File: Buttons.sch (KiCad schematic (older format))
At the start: 24 parts, among them SW1 SW_PUSHBUTTON, SW2 SW_PUSHBUTTON, SW3 SW_PUSHBUTTON, SW4 SW_PUSHBUTTON, SW5 SW_PUSHBUTTON, SW6 SW_PUSHBUTTON

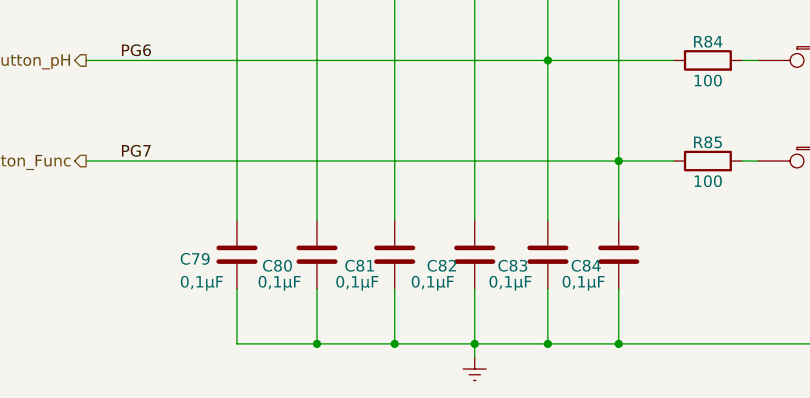
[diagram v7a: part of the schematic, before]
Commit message: corrected few footprints, correct all resistors and capacitors type for ordering
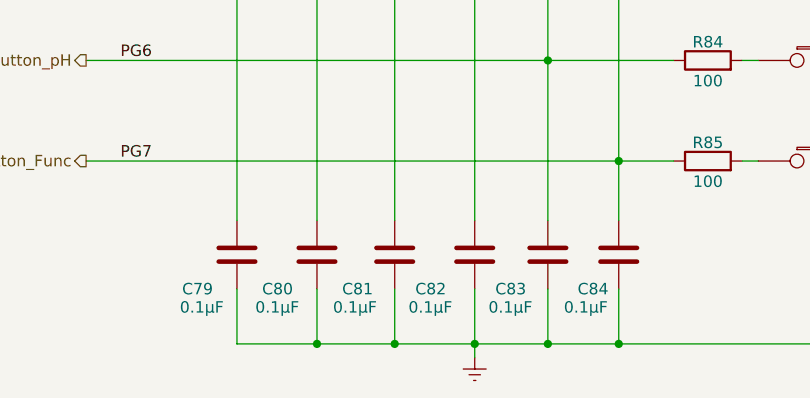
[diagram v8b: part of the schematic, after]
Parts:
- C79, C81, C82, C83, C84: value 0,1µF -> 0.1µF; Type C0603C104K5RACTU -> CL10B104KC8NNNC
- C80: value 0,1µF -> 0.1µF; Type CL10B105KA8NNNC -> CL10B104KC8NNNC
- R74, R75, R76, R77, R78, R79: Type (none) -> RC0805FR-0715KL
- R80, R81, R82, R83, R84, R85: Type (none) -> RC0805FR-07100RL
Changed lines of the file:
@@
 F 2 "Resistor_SMD:R_0805_2012Metric_Pad1.20x1.40mm_HandSolder" V 5930 1480 50  0001 C CNN
 F 3 "~" H 6000 1480 50  0001 C CNN
+F 4 "RC0805FR-0715KL" H 6000 1480 50  0001 C CNN "Type"
 	1    6000 1480
 	1    0    0    -1
@@
 F 2 "Resistor_SMD:R_0805_2012Metric_Pad1.20x1.40mm_HandSolder" V 5620 1480 50  0001 C CNN
 F 3 "~" H 5690 1480 50  0001 C CNN
+F 4 "RC0805FR-0715KL" H 5690 1480 50  0001 C CNN "Type"
 	1    5690 1480
 	1    0    0    -1
@@
 F 2 "Resistor_SMD:R_0805_2012Metric_Pad1.20x1.40mm_HandSolder" V 5300 1480 50  0001 C CNN
 F 3 "~" H 5370 1480 50  0001 C CNN
+F 4 "RC0805FR-0715KL" H 5370 1480 50  0001 C CNN "Type"
 	1    5370 1480
 	1    0    0    -1
@@
 F 2 "Resistor_SMD:R_0805_2012Metric_Pad1.20x1.40mm_HandSolder" V 4950 1480 50  0001 C CNN
 F 3 "~" H 5020 1480 50  0001 C CNN
+F 4 "RC0805FR-0715KL" H 5020 1480 50  0001 C CNN "Type"
 	1    5020 1480
 	1    0    0    -1
@@
 F 2 "Resistor_SMD:R_0805_2012Metric_Pad1.20x1.40mm_HandSolder" V 4610 1480 50  0001 C CNN
 F 3 "~" H 4680 1480 50  0001 C CNN
+F 4 "RC0805FR-0715KL" H 4680 1480 50  0001 C CNN "Type"
 	1    4680 1480
 	1    0    0    -1
@@
 F 2 "Resistor_SMD:R_0805_2012Metric_Pad1.20x1.40mm_HandSolder" V 4260 1480 50  0001 C CNN
 F 3 "~" H 4330 1480 50  0001 C CNN
+F 4 "RC0805FR-0715KL" H 4330 1480 50  0001 C CNN "Type"
 	1    4330 1480
 	1    0    0    -1
@@
 F 2 "Resistor_SMD:R_0805_2012Metric_Pad1.20x1.40mm_HandSolder" V 6310 2030 50  0001 C CNN
 F 3 "~" H 6380 2030 50  0001 C CNN
+F 4 "RC0805FR-07100RL" V 6380 2030 50  0001 C CNN "Type"
 	1    6380 2030
 	0    -1   -1   0
@@
 AR Path="/60D8C564/60D436EA" Ref="C?"  Part="1"
 AR Path="/60CDBD15/60D436EA" Ref="C79"  Part="1"
-F 0 "C79" H 4080 4620 50  0000 L CNN
-F 1 "0,1µF" H 4080 4520 50  0000 L CNN
+F 0 "C79" H 4090 4490 50  0000 L CNN
+F 1 "0.1µF" H 4080 4410 50  0000 L CNN
 F 2 "Capacitor_SMD:C_0603_1608Metric_Pad1.08x0.95mm_HandSolder" H 4368 4490 50  0001 C CNN
 F 3 "http://www.farnell.com/datasheets/2710676.pdf" H 4330 4640 50  0001 C CNN
-F 4 "C0603C104K5RACTU" H 4330 4640 50  0001 C CNN "Type"
+F 4 "CL10B104KC8NNNC" H 4330 4640 50  0001 C CNN "Type"
 	1    4330 4640
 	1    0    0    -1
@@
 AR Path="/60D8C564/60D44563" Ref="C?"  Part="1"
 AR Path="/60CDBD15/60D44563" Ref="C80"  Part="1"
-F 0 "C80" H 4440 4590 50  0000 L CNN
-F 1 "0,1µF" H 4420 4520 50  0000 L CNN
+F 0 "C80" H 4440 4490 50  0000 L CNN
+F 1 "0.1µF" H 4410 4410 50  0000 L CNN
 F 2 "Capacitor_SMD:C_0603_1608Metric_Pad1.08x0.95mm_HandSolder" H 4718 4490 50  0001 C CNN
 F 3 "http://www.farnell.com/datasheets/2710676.pdf" H 4680 4640 50  0001 C CNN
-F 4 "CL10B105KA8NNNC" H 4680 4640 50  0001 C CNN "Type"
+F 4 "CL10B104KC8NNNC" H 4680 4640 50  0001 C CNN "Type"
 	1    4680 4640
 	1    0    0    -1
@@
 AR Path="/60D8C564/60D44905" Ref="C?"  Part="1"
 AR Path="/60CDBD15/60D44905" Ref="C81"  Part="1"
-F 0 "C81" H 4800 4590 50  0000 L CNN
-F 1 "0,1µF" H 4760 4520 50  0000 L CNN
+F 0 "C81" H 4790 4490 50  0000 L CNN
+F 1 "0.1µF" H 4750 4410 50  0000 L CNN
 F 2 "Capacitor_SMD:C_0603_1608Metric_Pad1.08x0.95mm_HandSolder" H 5058 4490 50  0001 C CNN
 F 3 "http://www.farnell.com/datasheets/2710676.pdf" H 5020 4640 50  0001 C CNN
-F 4 "C0603C104K5RACTU" H 5020 4640 50  0001 C CNN "Type"
+F 4 "CL10B104KC8NNNC" H 5020 4640 50  0001 C CNN "Type"
 	1    5020 4640
 	1    0    0    -1
@@
 AR Path="/60D8C564/60D44D94" Ref="C?"  Part="1"
 AR Path="/60CDBD15/60D44D94" Ref="C82"  Part="1"
-F 0 "C82" H 5160 4590 50  0000 L CNN
-F 1 "0,1µF" H 5090 4520 50  0000 L CNN
+F 0 "C82" H 5110 4490 50  0000 L CNN
+F 1 "0.1µF" H 5080 4410 50  0000 L CNN
 F 2 "Capacitor_SMD:C_0603_1608Metric_Pad1.08x0.95mm_HandSolder" H 5408 4490 50  0001 C CNN
 F 3 "http://www.farnell.com/datasheets/2710676.pdf" H 5370 4640 50  0001 C CNN
-F 4 "C0603C104K5RACTU" H 5370 4640 50  0001 C CNN "Type"
+F 4 "CL10B104KC8NNNC" H 5370 4640 50  0001 C CNN "Type"
 	1    5370 4640
 	1    0    0    -1
@@
 AR Path="/60D8C564/60D452B1" Ref="C?"  Part="1"
 AR Path="/60CDBD15/60D452B1" Ref="C83"  Part="1"
-F 0 "C83" H 5470 4590 50  0000 L CNN
-F 1 "0,1µF" H 5430 4520 50  0000 L CNN
+F 0 "C83" H 5460 4490 50  0000 L CNN
+F 1 "0.1µF" H 5430 4410 50  0000 L CNN
 F 2 "Capacitor_SMD:C_0603_1608Metric_Pad1.08x0.95mm_HandSolder" H 5728 4490 50  0001 C CNN
 F 3 "http://www.farnell.com/datasheets/2710676.pdf" H 5690 4640 50  0001 C CNN
-F 4 "C0603C104K5RACTU" H 5690 4640 50  0001 C CNN "Type"
+F 4 "CL10B104KC8NNNC" H 5690 4640 50  0001 C CNN "Type"
 	1    5690 4640
 	1    0    0    -1
@@
 AR Path="/60D8C564/60D456CF" Ref="C?"  Part="1"
 AR Path="/60CDBD15/60D456CF" Ref="C84"  Part="1"
-F 0 "C84" H 5790 4590 50  0000 L CNN
-F 1 "0,1µF" H 5750 4520 50  0000 L CNN
+F 0 "C84" H 5820 4490 50  0000 L CNN
+F 1 "0.1µF" H 5760 4410 50  0000 L CNN
 F 2 "Capacitor_SMD:C_0603_1608Metric_Pad1.08x0.95mm_HandSolder" H 6038 4490 50  0001 C CNN
 F 3 "http://www.farnell.com/datasheets/2710676.pdf" H 6000 4640 50  0001 C CNN
-F 4 "C0603C104K5RACTU" H 6000 4640 50  0001 C CNN "Type"
+F 4 "CL10B104KC8NNNC" H 6000 4640 50  0001 C CNN "Type"
 	1    6000 4640
 	1    0    0    -1
@@
 F 2 "Resistor_SMD:R_0805_2012Metric_Pad1.20x1.40mm_HandSolder" V 6320 2470 50  0001 C CNN
 F 3 "~" H 6390 2470 50  0001 C CNN
+F 4 "RC0805FR-07100RL" V 6390 2470 50  0001 C CNN "Type"
 	1    6390 2470
 	0    -1   -1   0
@@
 F 2 "Resistor_SMD:R_0805_2012Metric_Pad1.20x1.40mm_HandSolder" V 6320 2910 50  0001 C CNN
 F 3 "~" H 6390 2910 50  0001 C CNN
+F 4 "RC0805FR-07100RL" V 6390 2910 50  0001 C CNN "Type"
 	1    6390 2910
 	0    -1   -1   0
@@
 F 2 "Resistor_SMD:R_0805_2012Metric_Pad1.20x1.40mm_HandSolder" V 6320 3350 50  0001 C CNN
 F 3 "~" H 6390 3350 50  0001 C CNN
+F 4 "RC0805FR-07100RL" V 6390 3350 50  0001 C CNN "Type"
 	1    6390 3350
 	0    -1   -1   0
@@
 F 2 "Resistor_SMD:R_0805_2012Metric_Pad1.20x1.40mm_HandSolder" V 6320 3790 50  0001 C CNN
 F 3 "~" H 6390 3790 50  0001 C CNN
+F 4 "RC0805FR-07100RL" V 6390 3790 50  0001 C CNN "Type"
 	1    6390 3790
 	0    -1   -1   0
@@
 F 2 "Resistor_SMD:R_0805_2012Metric_Pad1.20x1.40mm_HandSolder" V 6320 4230 50  0001 C CNN
 F 3 "~" H 6390 4230 50  0001 C CNN
+F 4 "RC0805FR-07100RL" V 6390 4230 50  0001 C CNN "Type"
 	1    6390 4230
 	0    -1   -1   0
